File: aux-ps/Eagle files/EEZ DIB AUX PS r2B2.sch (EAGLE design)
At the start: 122 parts, among them IC1 MAX31760AEE+, IC2 VIPer35L, IC3 TL431, J1 PF0030/PC, J2 1-726388-2, J3 1-726388-2, J4 1-726388-2, J5 SWEB 8094 AU/GN, Q1 BTA26-600, Q2 BTA26-600, Q3 2N7002, Q4 2N7002, Q5 2N7002, Q6 PSMN0R9-25YLC, SW1 DF62J12S2AHQA, X1 39-28-1063, X2 39-30-1039, X3 ZL231-16KG, X4 47053-1000, X5 47053-1000, X6 22-23-2021

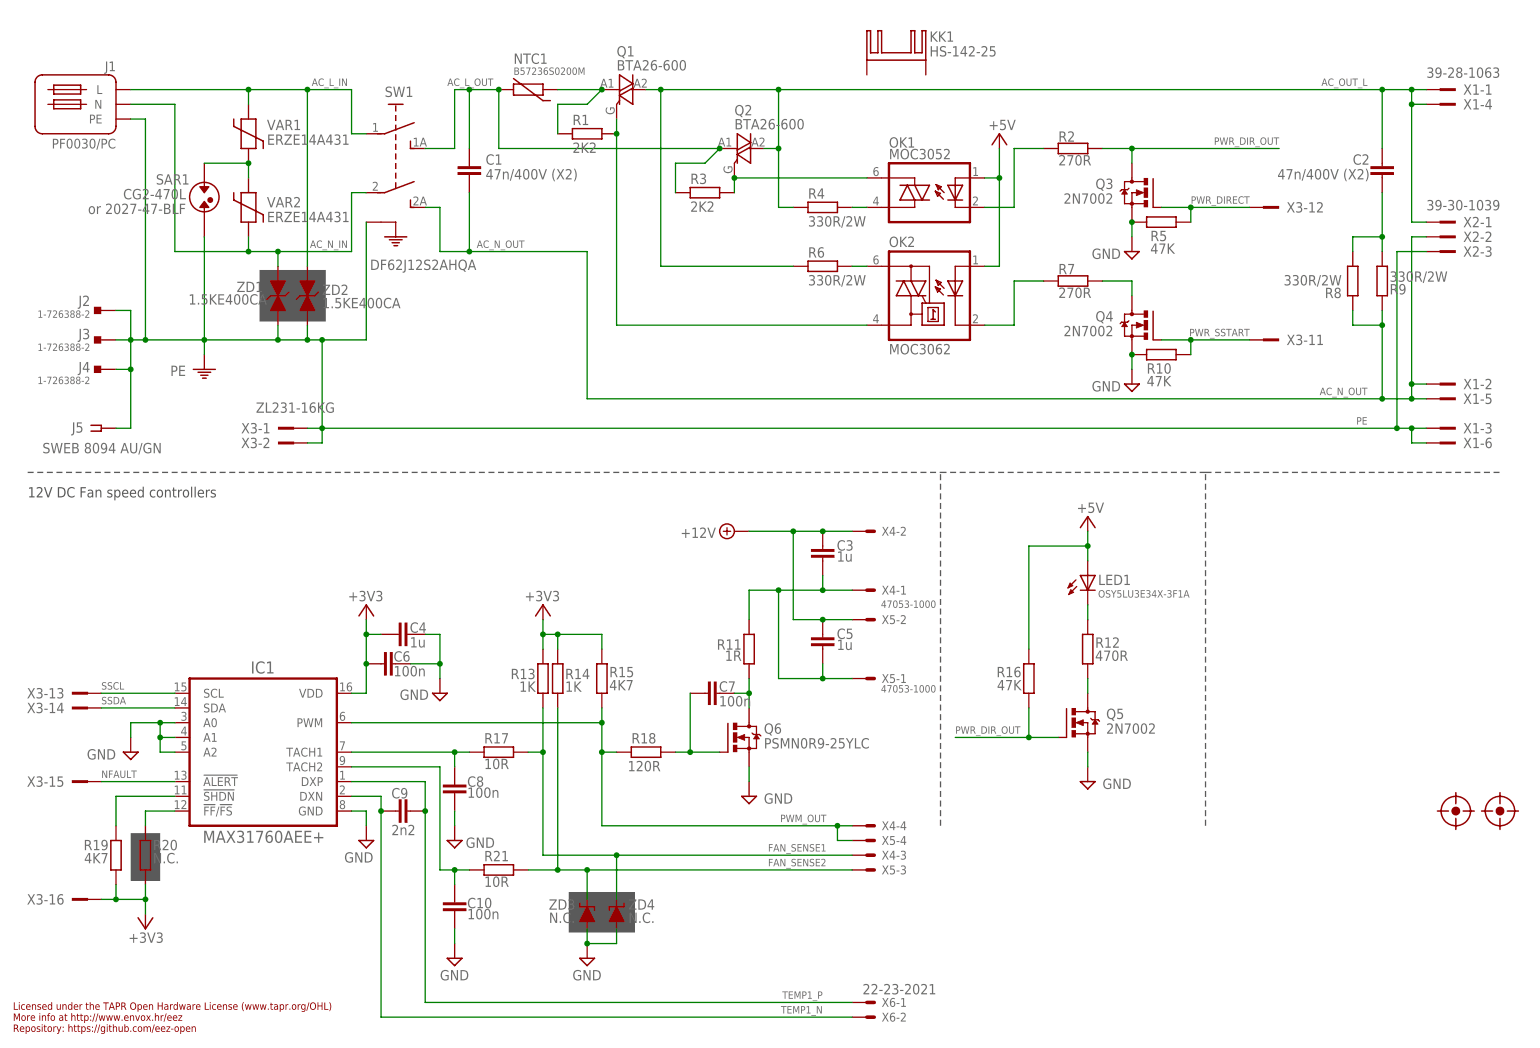
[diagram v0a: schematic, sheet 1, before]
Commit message: #33, optional 3V3 LDO
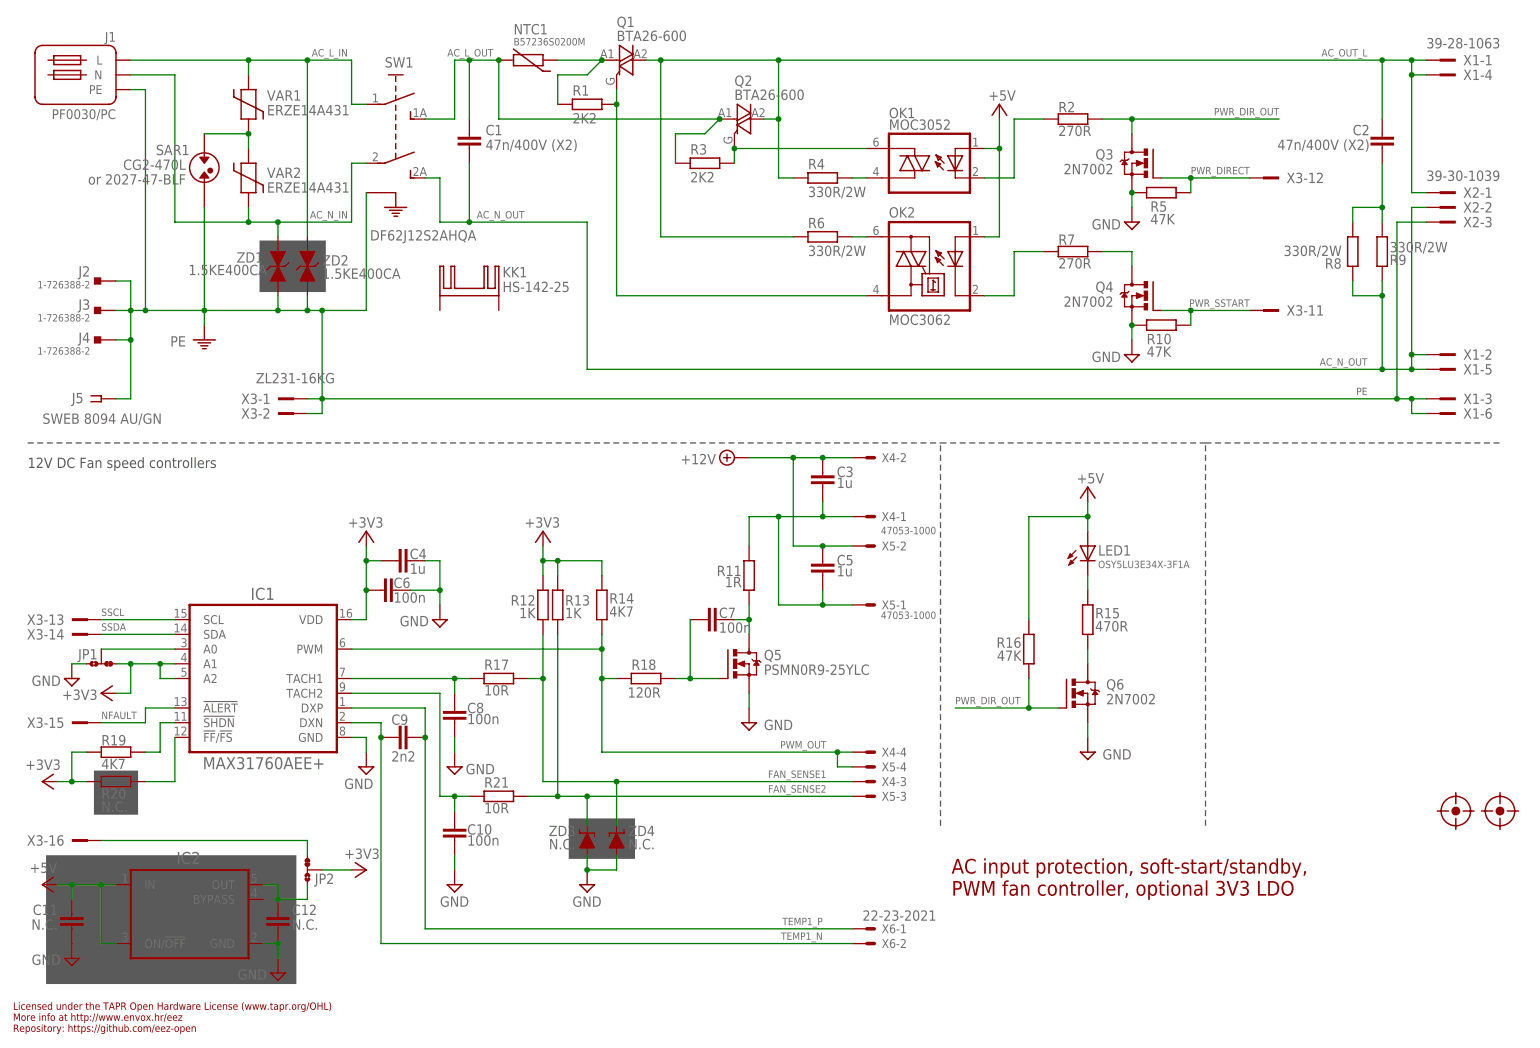
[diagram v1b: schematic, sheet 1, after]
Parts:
- added C29: 33n, rcl:C-EUC0805
- added C30: 2n2, rcl:C-EUC0805
- added IC4: TL431, EEZ_Lib1:TL431
- added JP3, JP4: JP3-CUT, EEZ_Lib1:JP3-CUT
- C11: value 2n2/1kV -> N.C.; device rcl:C-EUC1210 -> rcl:C-EUC0805
- C12: value UCY2G6R8MPD -> N.C.; device EEZ_Lib1:ECAP5G_10.5MM -> rcl:C-EUC0805
- C13: value UCY2G6R8MPD -> 2n2/1kV; device EEZ_Lib1:ECAP5G_10.5MM -> rcl:C-EUC1210
- C14: value 3n3 -> UCY2G6R8MPD; device rcl:C-EUC0805 -> EEZ_Lib1:ECAP5G_10.5MM
- C15: value UVZ1C471MPD -> UCY2G6R8MPD; device EEZ_Lib1:ECAP3.5G_8MM -> EEZ_Lib1:ECAP5G_10.5MM
- C16, C23: value 4u7 -> 3n3; device rcl:C-EUC1210 -> rcl:C-EUC0805
- C17: value 3n3 -> UVZ1C471MPD; device rcl:C-EUC0805 -> EEZ_Lib1:ECAP3.5G_8MM
- C18: value EEEFK1V470P -> 4u7; device EEZ_Lib1:ECAPPANASONIC_H -> rcl:C-EUC1210
- C19: value CY1Y-470P -> 3n3; device EEZ_Lib1:C-EUCY -> rcl:C-EUC0805
- C20: value 100n -> EEEFK1V470P; device rcl:C-EUC0603 -> EEZ_Lib1:ECAPPANASONIC_H
- C21: value 3n3 -> CY1Y-470P; device rcl:C-EUC0805 -> EEZ_Lib1:C-EUCY
- C22: value 1500u/16V -> 100n; device EEZ_Lib1:ECAP5G_13MM -> rcl:C-EUC0603
- C24: value N.C. -> 1500u/16V; device rcl:C-EUC0805 -> EEZ_Lib1:ECAP5G_13MM
- C25: value 33n -> 4u7; device rcl:C-EUC0805 -> rcl:C-EUC1210
- C26: value 18p -> N.C.; device rcl:C-EUC0603 -> rcl:C-EUC0805
- C28: value 2n2 -> 18p; device rcl:C-EUC0805 -> rcl:C-EUC0603
- IC2: value VIPer35L -> (none); device EEZ_Lib1:VIPER35 -> EEZ_Lib1:LP2985
- IC3: value TL431 -> VIPer35L; device EEZ_Lib1:TL431 -> EEZ_Lib1:VIPER35
- Q5: value 2N7002 -> PSMN0R9-25YLC; device EEZ_Lib1:2N7002 -> EEZ_Lib1:N-MOSFETLFPAK; MPN 2N7002-7-F -> (none); OC_FARNELL 1713823 -> (none); OC_NEWARK 25R5679 -> (none); PACKAGE SOT-23-3 -> (none); SUPPLIER DIODES INC. -> (none)
- Q6: value PSMN0R9-25YLC -> 2N7002; device EEZ_Lib1:N-MOSFETLFPAK -> EEZ_Lib1:2N7002; MPN (none) -> 2N7002-7-F; OC_FARNELL (none) -> 1713823; OC_NEWARK (none) -> 25R5679; PACKAGE (none) -> SOT-23-3; SUPPLIER (none) -> DIODES INC.
- R12: value 470R -> 1K
- R14: value 1K -> 4K7
- R15: value 4K7 -> 470R
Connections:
- new net N$19: JP2.NC, X3-16.1
- new net N$23: IC1.A0, JP1.COM
- new net N$24: C12.1, IC2.OUT, JP2.NO
- net +12V: now also C18.1; no longer C16.1
- net +12V_REC: now also C17.+, JP4.NC; no longer C15.+, JP2.NC
- net +3V3: now also IC1.A1, IC1.A2, JP1.NC, JP2.COM, R12.2, R14.1; no longer R14.2, R15.1, X3-16.1
- net +5V: now also C11.1, C25.1, IC2.IN, IC2.ON/!OFF; no longer C23.1
- net +5V_REC: now also C24.+, JP4.NO; no longer C22.+, JP2.NO
- net 0V: now also C14.-, C15.-, C20.-, C22.1, C30.2, IC3.GND, JP3.NO; no longer C12.-, C13.-, C18.-, C20.1, C26.2, IC2.GND, JP1.NO
- net 12VAC: now also C16.2; no longer C14.2
- net 5VAC: now also C23.2; no longer C21.2
- net AUX: now also C19.2; no longer C17.2
- net AUX_OUT: now also C20.+, C22.2, IC3.VDD; no longer C18.+, C20.2, IC2.VDD
- net DC_BUS: now also C13.1, C15.+; no longer C11.1, C13.+
- net DRAIN: now also Q5.D; no longer Q6.D
- net FAN_SENSE1: now also R12.1; no longer R13.1
- net FAN_SENSE2: now also R13.1; no longer R14.1
- net FB1: now also C29.1, IC4.C; no longer C27.1, IC3.C
- net GND: now also C11.2, C12.2, C17.-, C18.2, C21.2, C24.-, C25.2, IC2.GND, IC4.A, JP1.NO; no longer C15.-, C16.2, C19.2, C22.-, C23.2, IC1.A0, IC1.A1, IC1.A2, IC3.A
- net N$12: now also JP4.COM; no longer JP2.COM
- net N$13: now also Q6.D, R15.2; no longer Q5.D, R12.2
- net N$137: now also C13.2; no longer C11.2
- net N$138: now also C27.2, C30.1, IC3.FB; no longer C25.2, C28.1, IC2.FB
- net N$14: now also R15.1; no longer R12.1
- net N$140: now also C19.1; no longer C17.1
- net N$141: now also C28.1, IC3.ZCD; no longer C26.1, IC2.ZCD
- net N$146: now also C23.1; no longer C21.1
- net N$148: now also C26.2, IC4.REF; no longer C24.2, IC3.REF
- net N$149: now also C26.1, C29.2; no longer C24.1, C27.2
- net N$15: now also Q5.G; no longer Q6.G
- net N$152: now also C27.1; no longer C25.1
- net N$20: now also IC3.BR; no longer IC2.BR
- net N$4: now also C21.1, JP3.COM; no longer C19.1, JP1.COM
- net N$8: now also C16.1; no longer C14.1
- net N$9: now also C14.+; no longer C12.+
- net PE: now also JP3.NC; no longer JP1.NC
- net PWM_OUT: now also R14.2; no longer R15.2
- net PWR_DIR_OUT: now also Q6.G; no longer Q5.G
- net VIPER_D: now also IC3.DRAIN; no longer IC2.DRAIN
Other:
- note added: "AC input protection, soft-start/standby, PWM fan controller, optional 3V3 LDO"
- note added: "I2C address: 0xAE (optional 0xAC)"
- note added: "QR flyback bias power supply"
- note removed: "AC input, QR flyback bias power supply"
- note removed: "I2C address: 0xA0"
- moved on the sheet: C1, C10, C15, C16, C19, C2, C21, C23, C25, C26, C27, C28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

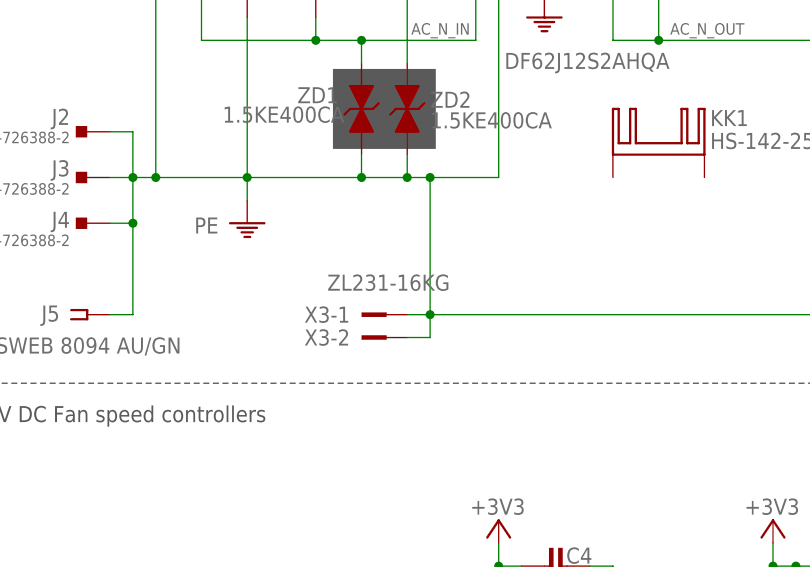
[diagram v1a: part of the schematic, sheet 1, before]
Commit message: X3 changed to vertical
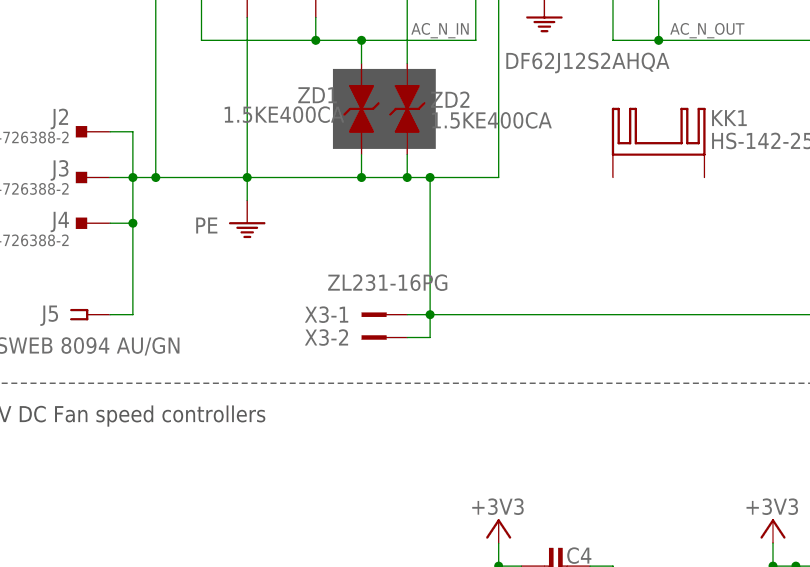
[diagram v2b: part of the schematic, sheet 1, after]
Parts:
- X3: value ZL231-16KG -> ZL231-16PG; device EEZ_connectors:IDC-16PIN-ANGLED -> EEZ_connectors:IDC-16PIN
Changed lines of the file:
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@@
 <part name="SUPPLY72" library="supply2" deviceset="GND" device=""/>
 <part name="SUPPLY50" library="supply2" deviceset="GND" device=""/>
-<part name="X3" library="EEZ_connectors" deviceset="IDC-16PIN" device="-ANGLED" value="ZL231-16KG"/>
+<part name="X3" library="EEZ_connectors" deviceset="IDC-16PIN" device="" value="ZL231-16PG"/>
 <part name="SUPPLY1" library="supply2" deviceset="+12V" device=""/>
 <part name="X6" library="con-molex" deviceset="22-23-2021" device=""/>
